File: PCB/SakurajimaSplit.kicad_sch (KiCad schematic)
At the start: 0 parts

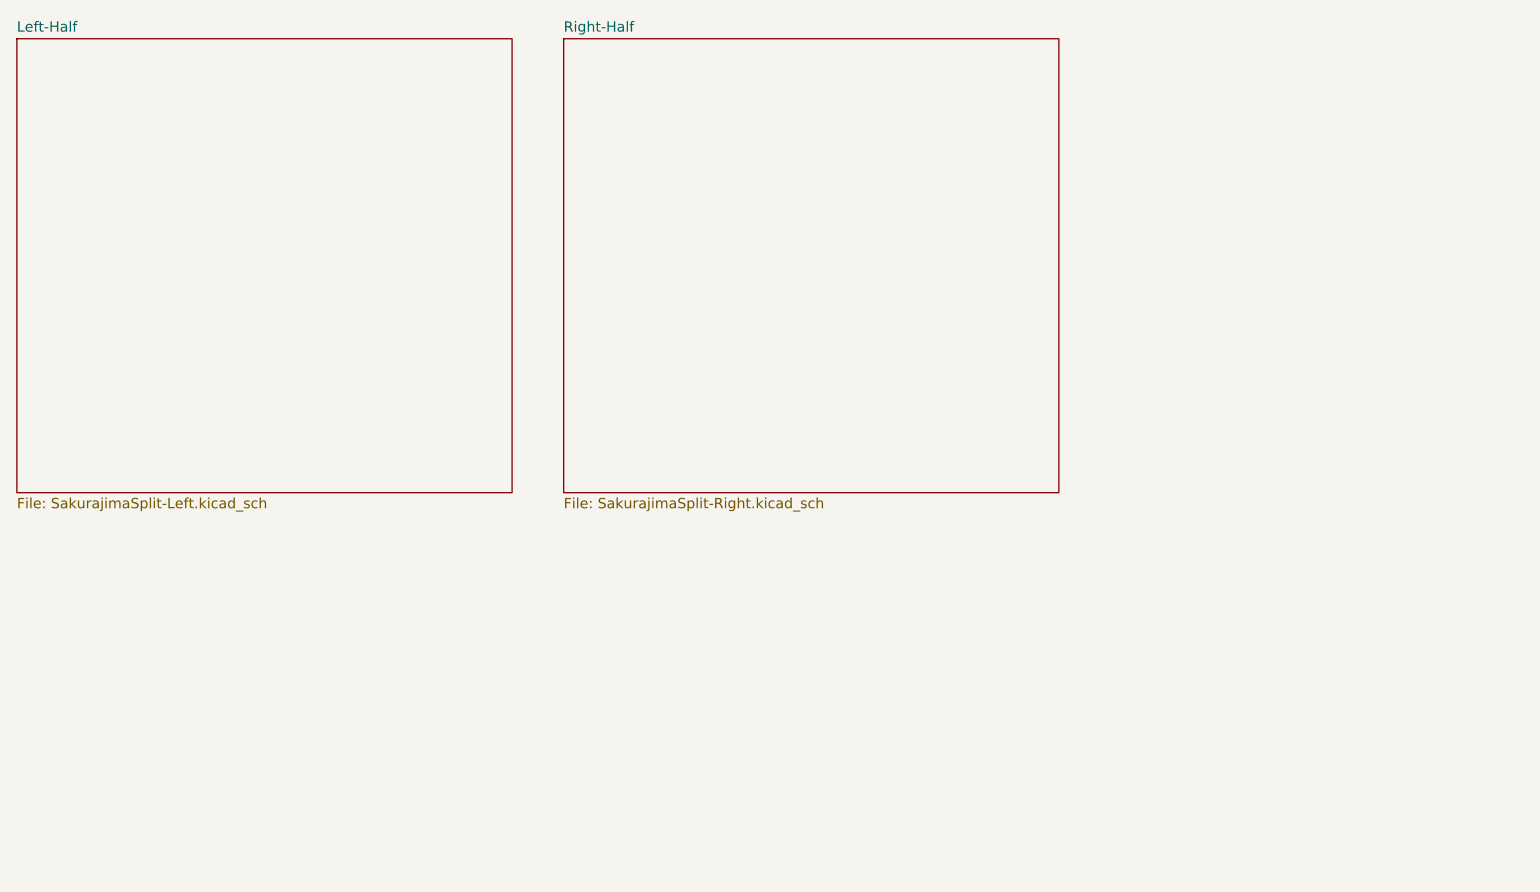
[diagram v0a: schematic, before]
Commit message: feat(sch): add USB to right-half circuit
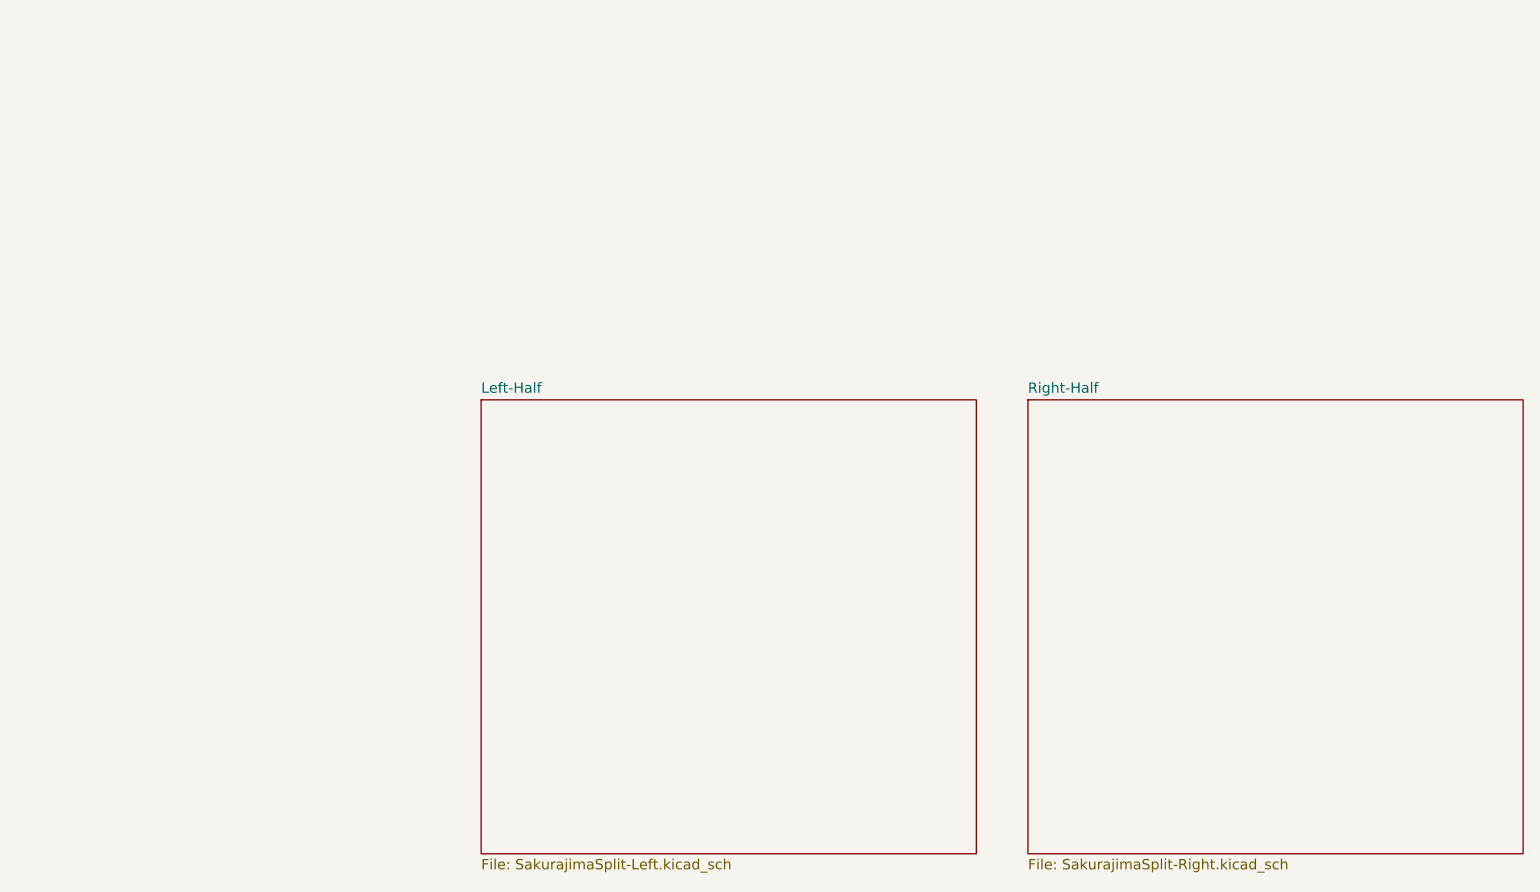
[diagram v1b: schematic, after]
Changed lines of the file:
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@@
 	(generator "eeschema")
 	(generator_version "9.0")
-	(paper "A4")
+	(paper "A3")
 	(title_block
 		(title "SakurajimaSplit")
@@
 	)
 	(sheet
-		(at 157.48 69.85)
+		(at 214.63 114.3)
 		(size 60.96 55.88)
 		(exclude_from_sim no)
@@
 		)
 		(property "Sheetname" "Right-Half"
-			(at 157.48 69.1384 0)
+			(at 214.63 113.5884 0)
 			(effects
 				(font
@@
 		)
 		(property "Sheetfile" "SakurajimaSplit-Right.kicad_sch"
-			(at 157.48 126.3146 0)
+			(at 214.63 170.7646 0)
 			(effects
 				(font
@@
 	)
 	(sheet
-		(at 90.17 69.85)
+		(at 147.32 114.3)
 		(size 60.96 55.88)
 		(exclude_from_sim no)
@@
 		)
 		(property "Sheetname" "Left-Half"
-			(at 90.17 69.1384 0)
+			(at 147.32 113.5884 0)
 			(effects
 				(font
@@
 		)
 		(property "Sheetfile" "SakurajimaSplit-Left.kicad_sch"
-			(at 90.17 126.3146 0)
+			(at 147.32 170.7646 0)
 			(effects
 				(font
